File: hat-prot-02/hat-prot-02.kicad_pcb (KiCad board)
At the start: 2 copper layers, 92 x 56 mm, 22 parts, among them J1 Conn_01x10_Male, J2 Conn_01x12_Male, J3 Conn_01x05_Male, J4 CR22A-60D-2.54DS_70_, J5 SolderJumper_2_Open, J6 SolderJumper_2_Open, J7 SolderJumper_2_Open, Q1 2SC1815, Q2 2SC1815, SW1 SW_SPDT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

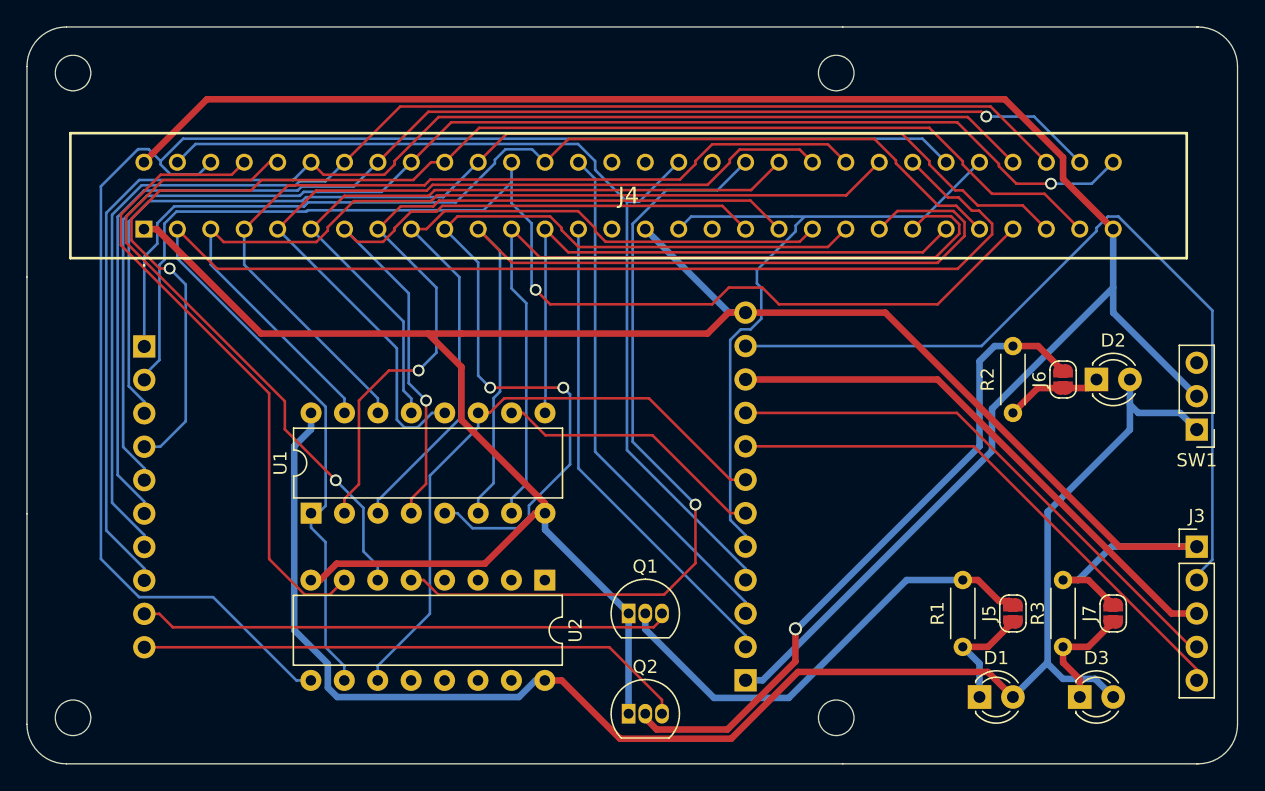
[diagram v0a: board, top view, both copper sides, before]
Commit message: modify design delete copy add QR code
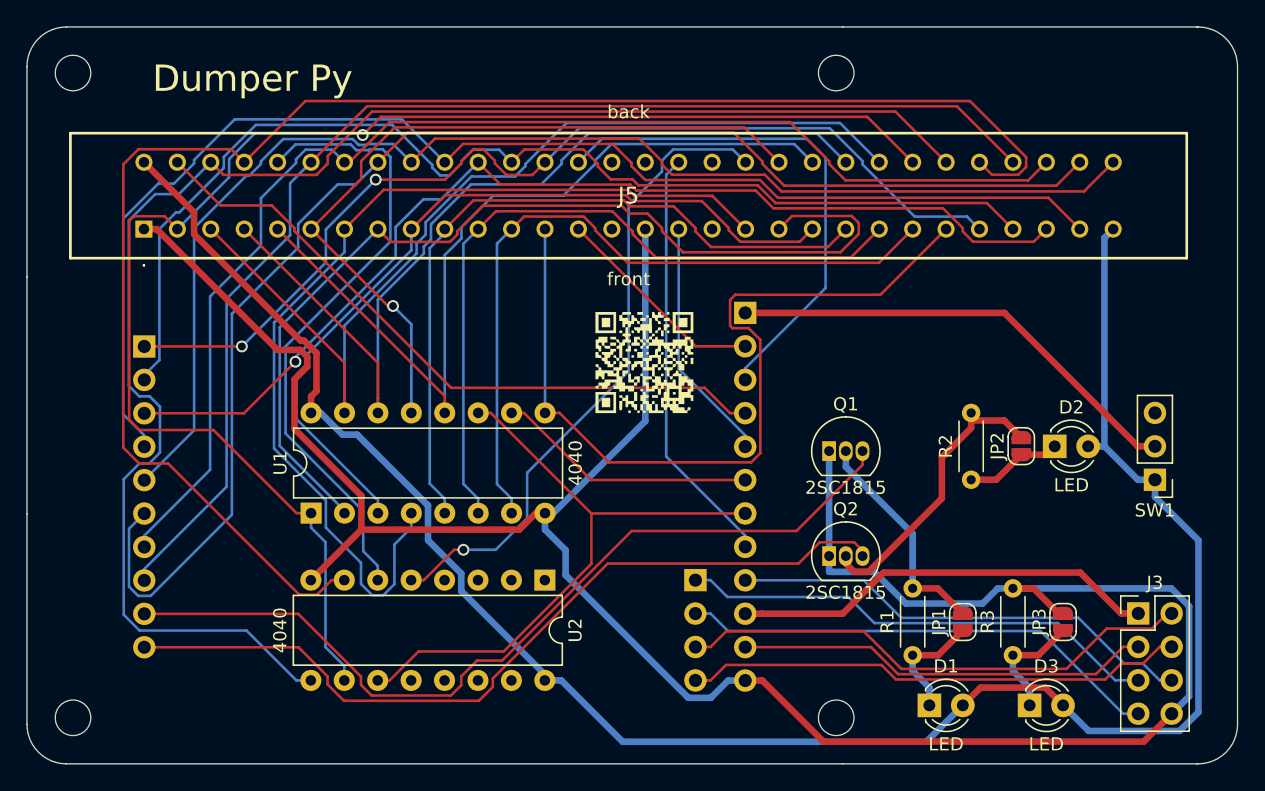
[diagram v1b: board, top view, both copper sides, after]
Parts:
- removed the J5 at (174.9, 88.6)
- removed J6, J7: SolderJumper_2_Open, Jumper:SolderJumper-2_P1.3mm_Open_RoundedPad1.0x1.5mm
- added G***: LOGO, SamacSys_Parts:QR_code_8_5, F.Cu at (147.0, 69.5)
- added J4: Conn_01x04_Female, Connector_PinSocket_2.54mm:PinSocket_1x04_P2.54mm_Vertical, B.Cu at (150.8, 86.0)
- added JP1: SolderJumper_2_Open, Jumper:SolderJumper-2_P1.3mm_Open_RoundedPad1.0x1.5mm, F.Cu at (171.1, 89.2)
- added JP2: SolderJumper_2_Open, Jumper:SolderJumper-2_P1.3mm_Open_RoundedPad1.0x1.5mm, F.Cu at (175.6, 75.9)
- added JP3: SolderJumper_2_Open, Jumper:SolderJumper-2_P1.3mm_Open_RoundedPad1.0x1.5mm, F.Cu at (178.7, 89.2)
- J1: value Conn_01x10_Male -> Conn_01x10_Female
- J2: value Conn_01x12_Male -> Conn_01x12_Female
- J3: value Conn_01x05_Male -> Conn_02x04_Odd_Even; footprint Connector_PinHeader_2.54mm:PinHeader_1x05_P2.54mm_Vertical -> Connector_PinHeader_2.54mm:PinHeader_2x04_P2.54mm_Vertical
- moved J2 27.9 mm to (154.6, 65.7), turned to 180 degrees
- moved Q1 19.6 mm to (161.0, 76.2)
- moved Q2 19.4 mm to (161.0, 84.2)
- moved J3 6.75 mm to (184.5, 88.6)
- moved D2 5.99 mm to (178.1, 75.9)
- moved R2 5.99 mm to (171.8, 78.4)
- moved SW1 4.96 mm to (185.7, 78.4)
- moved D3 3.86 mm to (176.2, 95.6)
- moved R1 3.86 mm to (167.3, 91.7)
- moved R3 3.86 mm to (174.9, 91.7)
- moved D1 3.86 mm to (168.6, 95.6)
- renumbered J4 to J5
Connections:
- net ADR15 renamed /PPU/A13
- J2 pad 11: EIO_2 -> EIO_0
- J2 pad 5: RST -> PPURD
- J2 pad 8: EIO_0 -> PPUWR
- J2 pad 9: EIO_1 -> EXT
- J3 pad 1: GND -> PWR3
- J3 pad 2: EIO_2 -> EIO_3
- J3 pad 3: PWR3 -> EIO_0
- J3 pad 4: EIO_1 -> EIO_4
- J3 pad 5: EIO_0 -> EIO_1
- J5 pad A17: RST -> PPURD
- J5 pad A30: VIN -> PWR
- J5 pad B1: VIN -> PWR
- J5 pad B17: WE -> PPUWR
- J5 pad B26: RST -> ADR13
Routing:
- net VIN: track 138.2 -> 35.3 mm
- net ADR13: track 49.1 -> 121.5 mm
- net RST: track 53.5 -> 0.00 mm
- net EIO_3: track 0.00 -> 39.6 mm
- net EIO_4: track 0.00 -> 38.2 mm
- net EXT: track 0.00 -> 35.6 mm
- net PPUWR: track 0.00 -> 32.1 mm
- net PWR: track 119.8 -> 151.0 mm
- net Net-(JP2-Pad2): track 50.5 -> 22.2 mm, vias 1 -> 0
- net EIO_2: track 63.6 -> 36.8 mm
- net PWM0: track 40.4 -> 66.2 mm
- net WE: track 74.6 -> 51.2 mm
- net OE: track 37.0 -> 16.4 mm
- net PWM1: track 42.1 -> 62.7 mm
- net Net-(JP1-Pad2): track 35.8 -> 17.1 mm
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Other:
- board text added: "Dumper Py"
- board text added: "back"
- board text added: "front"
- board text added: "https://github.com/km1ab/fc-dumper-py"

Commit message: update design
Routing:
- net Net-(JP2-Pad2): track 22.2 -> 23.2 mm
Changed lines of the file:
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@@
       (effects (font (size 1.27 1.27) (thickness 0.254)))
     )
-    (fp_text value "CR22A-60D-2.54DS_70_" (at 36.83 -2.54) (layer "F.SilkS") hide
+    (fp_text value "CR22A-60D-2.54DS_70_" (at 57.15 -2.54) (layer "F.SilkS")
       (effects (font (size 1.27 1.27) (thickness 0.254)))
     )
@@
   (segment (start 125.4149 82.2001) (end 125.4149 79.633) (width 0.5) (layer "F.Cu") (net 1))
   (segment (start 160.96 76.23) (end 160.96 84.21) (width 0.5) (layer "B.Cu") (net 1))
-  (segment (start 164.3881 85.4101) (end 160.96 85.4101) (width 0.5) (layer "B.Cu") (net 1))
-  (segment (start 173.7799 86.665) (end 172.6272 87.8177) (width 0.5) (layer "B.Cu") (net 1))
+  (segment (start 161.595 85.4101) (end 160.96 84.7751) (width 0.5) (layer "B.Cu") (net 1))
+  (segment (start 166.7957 87.8177) (end 164.3881 85.4101) (width 0.5) (layer "B.Cu") (net 1))
   (segment (start 140.9354 83.7655) (end 140.9354 85.6554) (width 0.5) (layer "B.Cu") (net 1))
-  (segment (start 160.96 84.21) (end 160.96 85.4101) (width 0.5) (layer "B.Cu") (net 1))
   (segment (start 139.37 81.575) (end 139.37 82.2001) (width 0.5) (layer "B.Cu") (net 1))
   (segment (start 150.2618 94.9818) (end 151.9731 94.9818) (width 0.5) (layer "B.Cu") (net 1))
@@
   (segment (start 140.9354 85.6554) (end 150.2618 94.9818) (width 0.5) (layer "B.Cu") (net 1))
   (segment (start 188.3238 88.0166) (end 186.9722 86.665) (width 0.5) (layer "B.Cu") (net 1))
+  (segment (start 172.6272 87.8177) (end 166.7957 87.8177) (width 0.5) (layer "B.Cu") (net 1))
+  (segment (start 164.3881 85.4101) (end 161.595 85.4101) (width 0.5) (layer "B.Cu") (net 1))
   (segment (start 186.995 96.19) (end 188.3238 94.8612) (width 0.5) (layer "B.Cu") (net 1))
   (segment (start 139.37 80.95) (end 139.37 81.575) (width 0.5) (layer "B.Cu") (net 1))
@@
   (segment (start 146.99 73.955) (end 146.99 59.36) (width 0.5) (layer "B.Cu") (net 1))
   (segment (start 186.9722 86.665) (end 174.93 86.665) (width 0.5) (layer "B.Cu") (net 1))
-  (segment (start 172.6272 87.8177) (end 166.7957 87.8177) (width 0.5) (layer "B.Cu") (net 1))
-  (segment (start 166.7957 87.8177) (end 164.3881 85.4101) (width 0.5) (layer "B.Cu") (net 1))
+  (segment (start 173.7799 86.665) (end 172.6272 87.8177) (width 0.5) (layer "B.Cu") (net 1))
   (segment (start 151.9731 94.9818) (end 153.2849 93.67) (width 0.5) (layer "B.Cu") (net 1))
   (segment (start 154.585 93.67) (end 153.2849 93.67) (width 0.5) (layer "B.Cu") (net 1))
   (segment (start 139.37 81.575) (end 146.99 73.955) (width 0.5) (layer "B.Cu") (net 1))
+  (segment (start 160.96 84.7751) (end 160.96 84.21) (width 0.5) (layer "B.Cu") (net 1))
   (segment (start 108.5526 74.63) (end 107.7648 73.8422) (width 0.2) (layer "F.Cu") (net 2))
   (segment (start 125.5137 52.2136) (end 126.8986 50.8287) (width 0.2) (layer "F.Cu") (net 2))
@@
   (segment (start 139.37 72.2299) (end 139.37 59.36) (width 0.2) (layer "B.Cu") (net 15))
   (segment (start 139.37 73.33) (end 139.37 72.2299) (width 0.2) (layer "B.Cu") (net 15))
-  (segment (start 167.31 91.745) (end 169.245 91.745) (width 0.5) (layer "F.Cu") (net 16))
-  (segment (start 169.245 91.745) (end 171.12 89.87) (width 0.5) (layer "F.Cu") (net 16))
+  (segment (start 167.31 91.745) (end 168.58 90.475) (width 0.5) (layer "F.Cu") (net 16))
+  (segment (start 170.515 90.475) (end 171.12 89.87) (width 0.5) (layer "F.Cu") (net 16))
+  (segment (start 168.58 90.475) (end 170.515 90.475) (width 0.5) (layer "F.Cu") (net 16))
   (segment (start 167.31 91.745) (end 167.31 92.9349) (width 0.5) (layer "B.Cu") (net 16))
   (segment (start 168.58 95.555) (end 168.58 94.2049) (width 0.5) (layer "B.Cu") (net 16))
@@
   (segment (start 121.59 73.33) (end 122.3221 73.33) (width 0.5) (layer "B.Cu") (net 18))
   (segment (start 181.8849 75.87) (end 181.8849 60.0251) (width 0.5) (layer "B.Cu") (net 18))
+  (segment (start 180.6842 97.4992) (end 187.601 97.4992) (width 0.5) (layer "B.Cu") (net 18))
   (segment (start 181.8849 75.87) (end 184.4249 78.41) (width 0.5) (layer "B.Cu") (net 18))
   (segment (start 133.005 86.86) (end 139.805 93.66) (width 0.5) (layer "B.Cu") (net 18))
   (segment (start 125.0944 74.9837) (end 130.48 80.3693) (width 0.5) (layer "B.Cu") (net 18))
   (segment (start 185.725 78.41) (end 184.4249 78.41) (width 0.5) (layer "B.Cu") (net 18))
-  (segment (start 180.6842 97.4992) (end 187.601 97.4992) (width 0.5) (layer "B.Cu") (net 18))
   (segment (start 139.805 93.66) (end 140.6051 93.66) (width 0.5) (layer "B.Cu") (net 18))
   (segment (start 139.355 93.66) (end 139.805 93.66) (width 0.5) (layer "B.Cu") (net 18))
+  (segment (start 187.601 97.4992) (end 189.0279 96.0723) (width 0.5) (layer "B.Cu") (net 18))
   (segment (start 130.48 80.3693) (end 130.48 83.011) (width 0.5) (layer "B.Cu") (net 18))
+  (segment (start 189.0279 96.0723) (end 189.0279 81.7129) (width 0.5) (layer "B.Cu") (net 18))
   (segment (start 168.3522 98.3228) (end 145.2679 98.3228) (width 0.5) (layer "B.Cu") (net 18))
   (segment (start 171.12 95.555) (end 168.3522 98.3228) (width 0.5) (layer "B.Cu") (net 18))
   (segment (start 130.48 83.011) (end 133.005 85.536) (width 0.5) (layer "B.Cu") (net 18))
-  (segment (start 187.601 97.4992) (end 189.0279 96.0723) (width 0.5) (layer "B.Cu") (net 18))
-  (segment (start 189.0279 83.013) (end 185.725 79.7101) (width 0.5) (layer "B.Cu") (net 18))
+  (segment (start 178.74 95.555) (end 180.6842 97.4992) (width 0.5) (layer "B.Cu") (net 18))
   (segment (start 145.2679 98.3228) (end 140.6051 93.66) (width 0.5) (layer "B.Cu") (net 18))
-  (segment (start 178.74 95.555) (end 180.6842 97.4992) (width 0.5) (layer "B.Cu") (net 18))
   (segment (start 122.3221 73.33) (end 123.9758 74.9837) (width 0.5) (layer "B.Cu") (net 18))
   (segment (start 123.9758 74.9837) (end 125.0944 74.9837) (width 0.5) (layer "B.Cu") (net 18))
-  (segment (start 185.725 78.41) (end 185.725 79.7101) (width 0.5) (layer "B.Cu") (net 18))
   (segment (start 133.005 85.536) (end 133.005 86.86) (width 0.5) (layer "B.Cu") (net 18))
-  (segment (start 189.0279 96.0723) (end 189.0279 83.013) (width 0.5) (layer "B.Cu") (net 18))
+  (segment (start 189.0279 81.7129) (end 185.725 78.41) (width 0.5) (layer "B.Cu") (net 18))
   (segment (start 181.8849 60.0251) (end 182.55 59.36) (width 0.5) (layer "B.Cu") (net 18))
   (segment (start 135.56 54.3667) (end 135.56 54.1674) (width 0.2) (layer "F.Cu") (net 19))
@@
   (segment (start 117.78 54.4129) (end 117.78 54.2065) (width 0.2) (layer "B.Cu") (net 29))
   (segment (start 116.9085 55.2844) (end 117.78 54.4129) (width 0.2) (layer "B.Cu") (net 29))
-  (segment (start 176.865 91.745) (end 178.74 89.87) (width 0.5) (layer "F.Cu") (net 30))
-  (segment (start 174.93 91.745) (end 176.865 91.745) (width 0.5) (layer "F.Cu") (net 30))
+  (segment (start 176.2 90.475) (end 178.135 90.475) (width 0.5) (layer "F.Cu") (net 30))
+  (segment (start 174.93 91.745) (end 176.2 90.475) (width 0.5) (layer "F.Cu") (net 30))
+  (segment (start 178.135 90.475) (end 178.74 89.87) (width 0.5) (layer "F.Cu") (net 30))
   (segment (start 174.93 92.9349) (end 174.93 91.745) (width 0.5) (layer "B.Cu") (net 30))
   (segment (start 176.2 95.555) (end 176.2 94.2049) (width 0.5) (layer "B.Cu") (net 30))
@@
   (segment (start 169.215 86.665) (end 171.12 88.57) (width 0.5) (layer "F.Cu") (net 60))
   (segment (start 167.31 86.665) (end 169.215 86.665) (width 0.5) (layer "F.Cu") (net 60))
+  (segment (start 165.405 80.6051) (end 165.405 84.76) (width 0.5) (layer "B.Cu") (net 60))
   (segment (start 162.23 76.23) (end 162.23 77.4301) (width 0.5) (layer "B.Cu") (net 60))
-  (segment (start 162.23 77.4301) (end 167.31 82.5101) (width 0.5) (layer "B.Cu") (net 60))
-  (segment (start 167.31 82.5101) (end 167.31 86.665) (width 0.5) (layer "B.Cu") (net 60))
-  (segment (start 171.755 74.4801) (end 171.755 73.905) (width 0.5) (layer "F.Cu") (net 61))
+  (segment (start 165.405 84.76) (end 167.31 86.665) (width 0.5) (layer "B.Cu") (net 60))
+  (segment (start 162.23 77.4301) (end 165.405 80.6051) (width 0.5) (layer "B.Cu") (net 60))
+  (segment (start 162.23 84.21) (end 162.23 84.7751) (width 0.5) (layer "F.Cu") (net 61))
+  (segment (start 169.5302 79.8262) (end 169.5302 74.2848) (width 0.5) (layer "F.Cu") (net 61))
+  (segment (start 162.23 84.7751) (end 162.865 85.4101) (width 0.5) (layer "F.Cu") (net 61))
+  (segment (start 170.485 73.33) (end 171.755 73.33) (width 0.5) (layer "F.Cu") (net 61))
   (segment (start 162.865 85.4101) (end 163.9463 85.4101) (width 0.5) (layer "F.Cu") (net 61))
-  (segment (start 169.5302 79.8262) (end 169.5302 76.7049) (width 0.5) (layer "F.Cu") (net 61))
-  (segment (start 169.5302 76.7049) (end 171.755 74.4801) (width 0.5) (layer "F.Cu") (net 61))
-  (segment (start 162.23 84.7751) (end 162.865 85.4101) (width 0.5) (layer "F.Cu") (net 61))
-  (segment (start 171.755 73.33) (end 171.755 73.905) (width 0.5) (layer "F.Cu") (net 61))
+  (segment (start 173.69 73.33) (end 175.565 75.205) (width 0.5) (layer "F.Cu") (net 61))
   (segment (start 163.9463 85.4101) (end 169.5302 79.8262) (width 0.5) (layer "F.Cu") (net 61))
-  (segment (start 171.755 73.905) (end 174.265 73.905) (width 0.5) (layer "F.Cu") (net 61))
-  (segment (start 174.265 73.905) (end 175.565 75.205) (width 0.5) (layer "F.Cu") (net 61))
-  (segment (start 162.23 84.21) (end 162.23 84.7751) (width 0.5) (layer "F.Cu") (net 61))
+  (segment (start 169.5302 74.2848) (end 170.485 73.33) (width 0.5) (layer "F.Cu") (net 61))
+  (segment (start 171.755 73.33) (end 173.69 73.33) (width 0.5) (layer "F.Cu") (net 61))
   (segment (start 129.195 86.04) (end 130.1576 86.04) (width 0.2) (layer "F.Cu") (net 62))
   (segment (start 132.4654 83.7322) (end 133.1686 83.7322) (width 0.2) (layer "F.Cu") (net 62))

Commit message: add version silk
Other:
- board text added: "202212"
- board text added: "Rev1.0"
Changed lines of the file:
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@@
+    (effects (font (size 1 1) (thickness 0.15)))
+  )
+  (gr_text "Rev1.0" (at 129.845 48.565) (layer "F.SilkS")
     (effects (font (size 1 1) (thickness 0.15)))
   )
@@
   (gr_text "Dumper Py" (at 117.145 47.93) (layer "F.SilkS")
     (effects (font (size 2 2) (thickness 0.3)))
+  )
+  (gr_text "202212" (at 146.355 74.6) (layer "F.SilkS")
+    (effects (font (size 1 1) (thickness 0.15)))
   )
   (gr_text "Extend PCB edge 0.5mm if using SMT header" (at 103 42.5) (layer "Dwgs.User")
@@
       (effects (font (size 1 1) (thickness 0.15)))
     )
+    (format (units 3) (units_format 1) (precision 4))
+    (style (thickness 0.1) (arrow_length 1.27) (text_position_mode 0) (extension_height 0.58642) (extension_offset 0.5) keep_text_aligned)
+  )
+  (dimension (type orthogonal) (layer "Dwgs.User")
+    (pts (xy 150.8 93.65) (xy 154.61 93.65))
+    (height 13.97)
+    (orientation 0)
+    (gr_text "3.8100 mm" (at 152.705 106.47) (layer "Dwgs.User")
+      (effects (font (size 1 1) (thickness 0.15)))
+    )
+    (format (units 3) (units_format 1) (precision 4))
+    (style (thickness 0.1) (arrow_length 1.27) (text_position_mode 0) (extension_height 0.58642) (extension_offset 0.5) keep_text_aligned)
+  )
+  (dimension (type orthogonal) (layer "Dwgs.User")
+    (pts (xy 150.8 91.11) (xy 150.8 100))
+    (height 0)
+    (orientation 1)
+    (gr_text "8.8900 mm" (at 149.65 95.555 90) (layer "Dwgs.User")
+      (effects (font (size 1 1) (thickness 0.15)))
+    )
